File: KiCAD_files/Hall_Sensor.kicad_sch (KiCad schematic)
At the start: 10 parts, among them J901 Conn_01x05, U901 Si8640BB-B-IS1

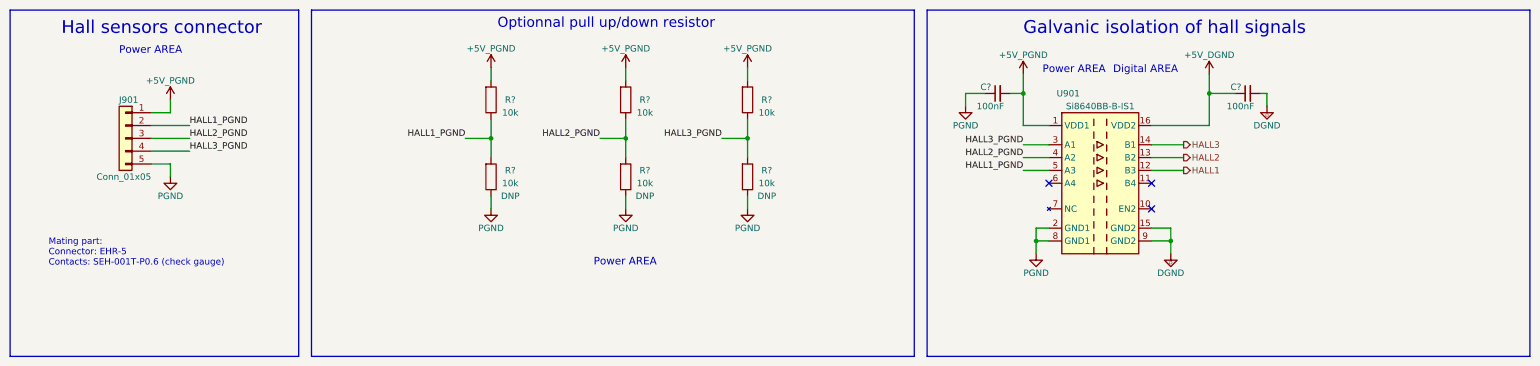
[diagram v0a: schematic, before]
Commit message: Added ERC rules for galvanic isolation. Modified SPIN pinout.
Signed-off-by: Jean Alinei <jean.alinei@laas.fr>
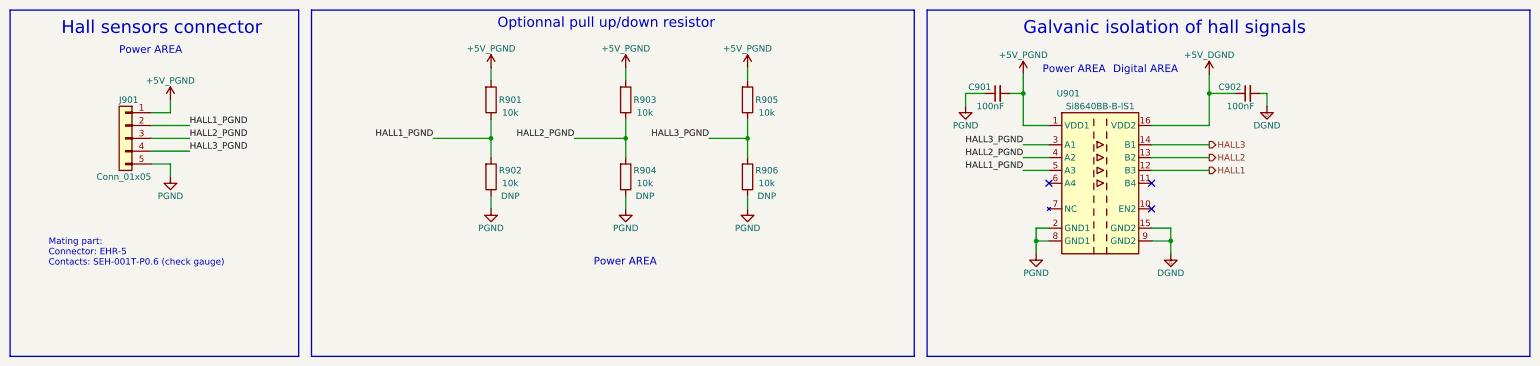
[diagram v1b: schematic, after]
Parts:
- gave numbers to parts that had none: 8
